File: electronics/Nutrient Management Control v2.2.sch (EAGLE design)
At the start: 16 parts, among them IC1 7407N, Q1 FQP30N06L

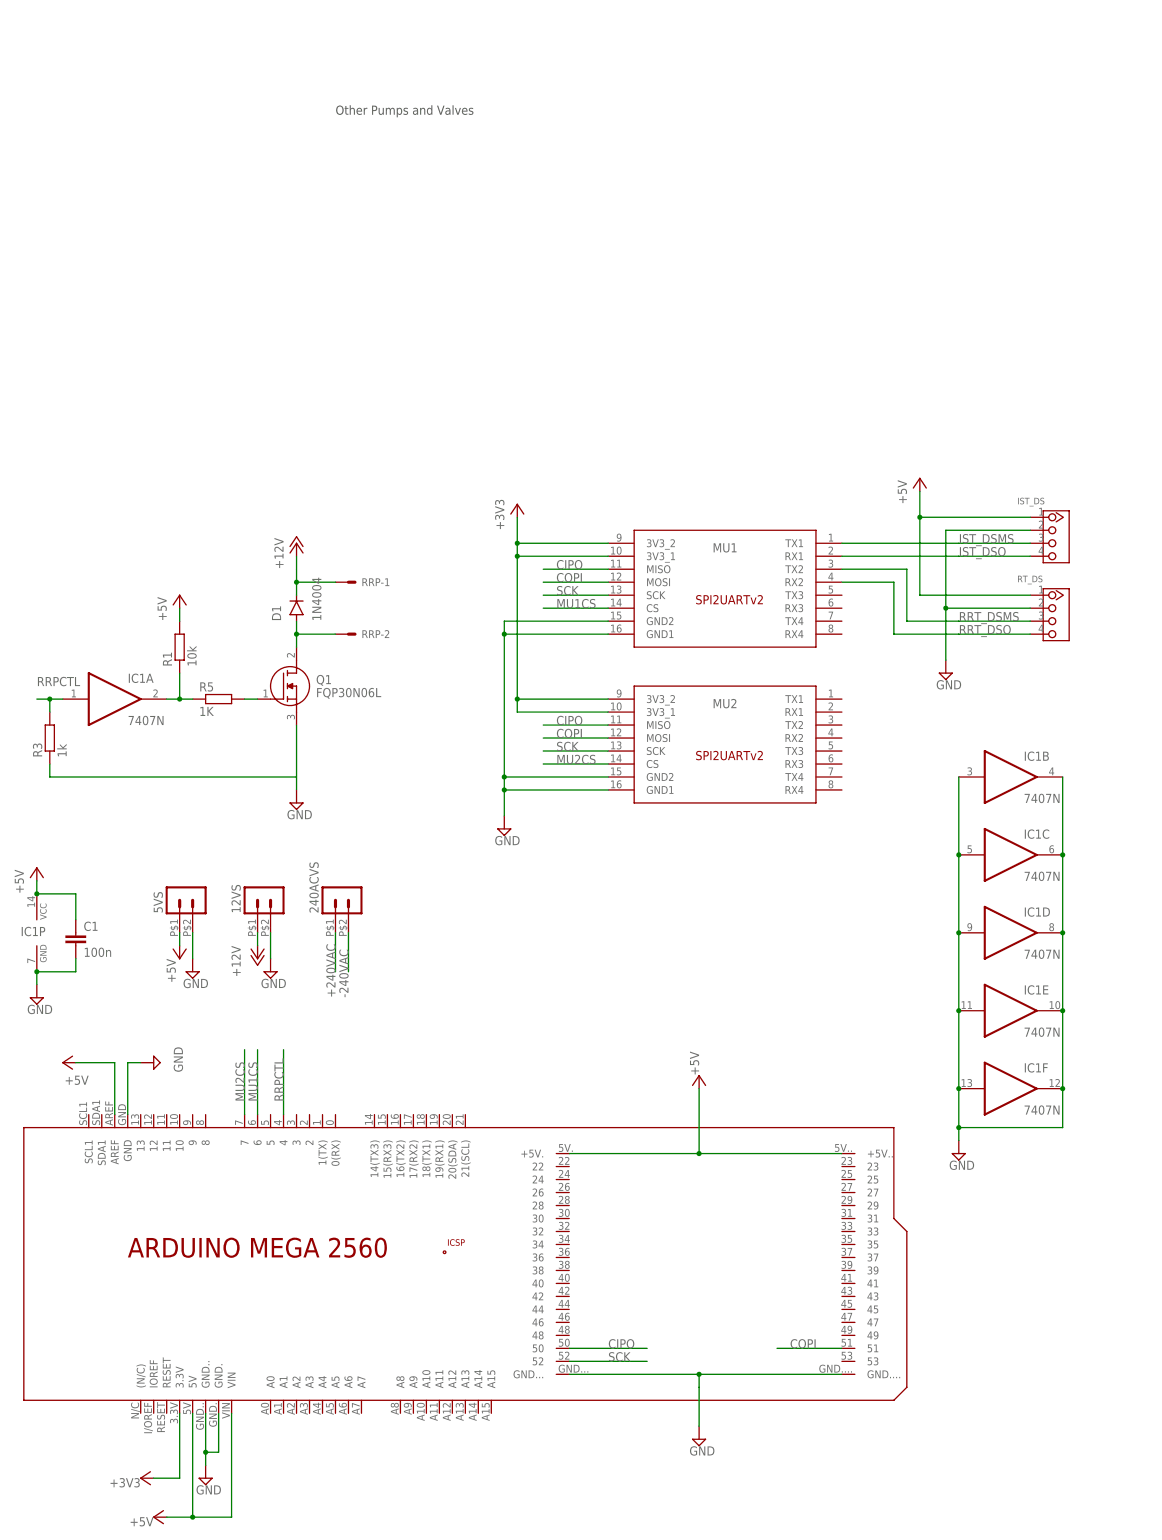
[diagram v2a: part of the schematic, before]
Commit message: Added UV Steriliser
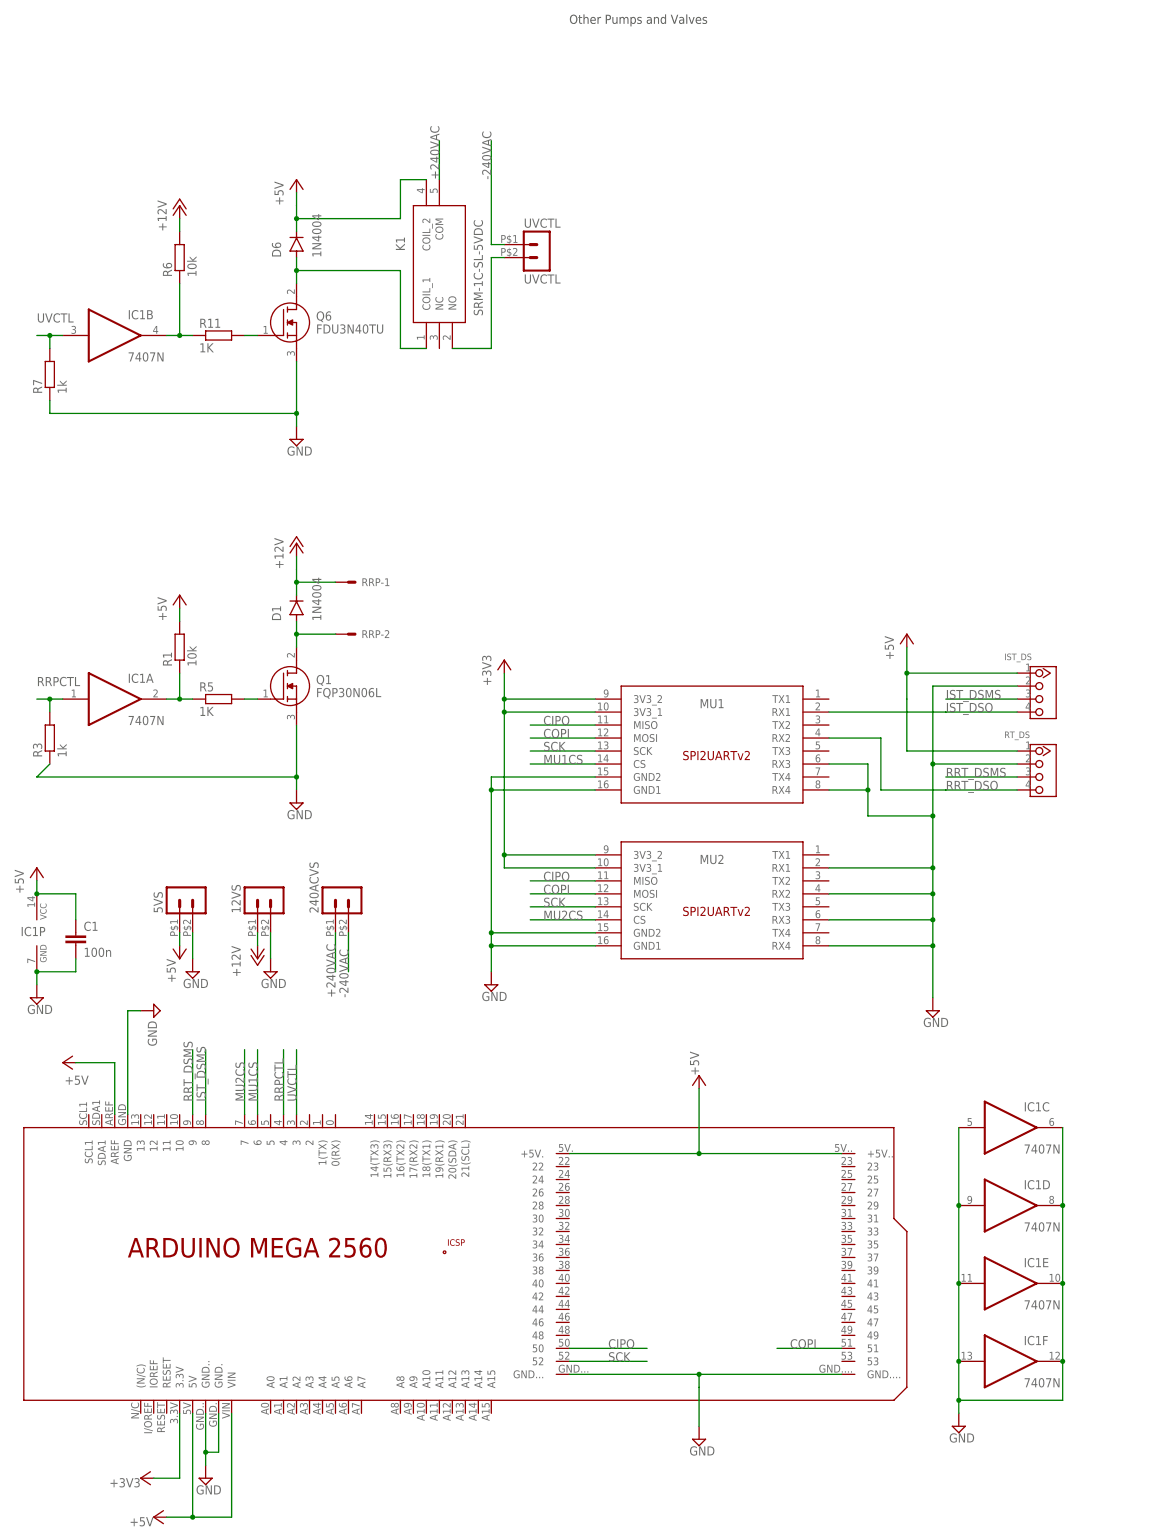
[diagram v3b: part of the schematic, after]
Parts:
- added D6: 1N4004, Aeroponics Control:1N4004
- added K1: SRM-1C-SL-5VDC, Aeroponics Control:SRM-1C-SL-5VDC
- added Q6: FDU3N40TU, Aeroponics Control:FDU3N40TU
- added R11: 1K, Aeroponics Control:R-EU_0204/7
- added R6: 10k, Aeroponics Control:R-EU_0204/7
- added R7: 1k, Aeroponics Control:R-EU_0204/7
- added UVCTL: UVCTL, Aeroponics Control:HEADER_POS2_43650-0215
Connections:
- new net N$13: Q6.G, R11.2
- new net N$17: IC1B.O, R11.1, R6.1
- new net N$21: D6.A, K1.COIL_1, Q6.D
- new net N$7: K1.NO, UVCTL.2
- new net UVCTL: IC1B.I, PCB2.3, R7.2
- net +12V: now also R6.2
- net +240VAC: now also K1.COM
- net +5V: now also D6.C, K1.COIL_2
- net -240VAC: now also UVCTL.1
- net GND: now also MU1.RX3, MU1.RX4, MU2.RX1, MU2.RX2, MU2.RX3, MU2.RX4, Q6.S, R7.1; no longer IC1B.I, IC1B.O
- net IST_DSMS: now also PCB2.8; no longer MU1.TX1
- net RRT_DSMS: now also PCB2.9; no longer MU1.TX2
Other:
- moved on the sheet: IC1B, IC1C, IC1D, IC1E, IC1F, IST_DS, MU1, MU2, RT_DS

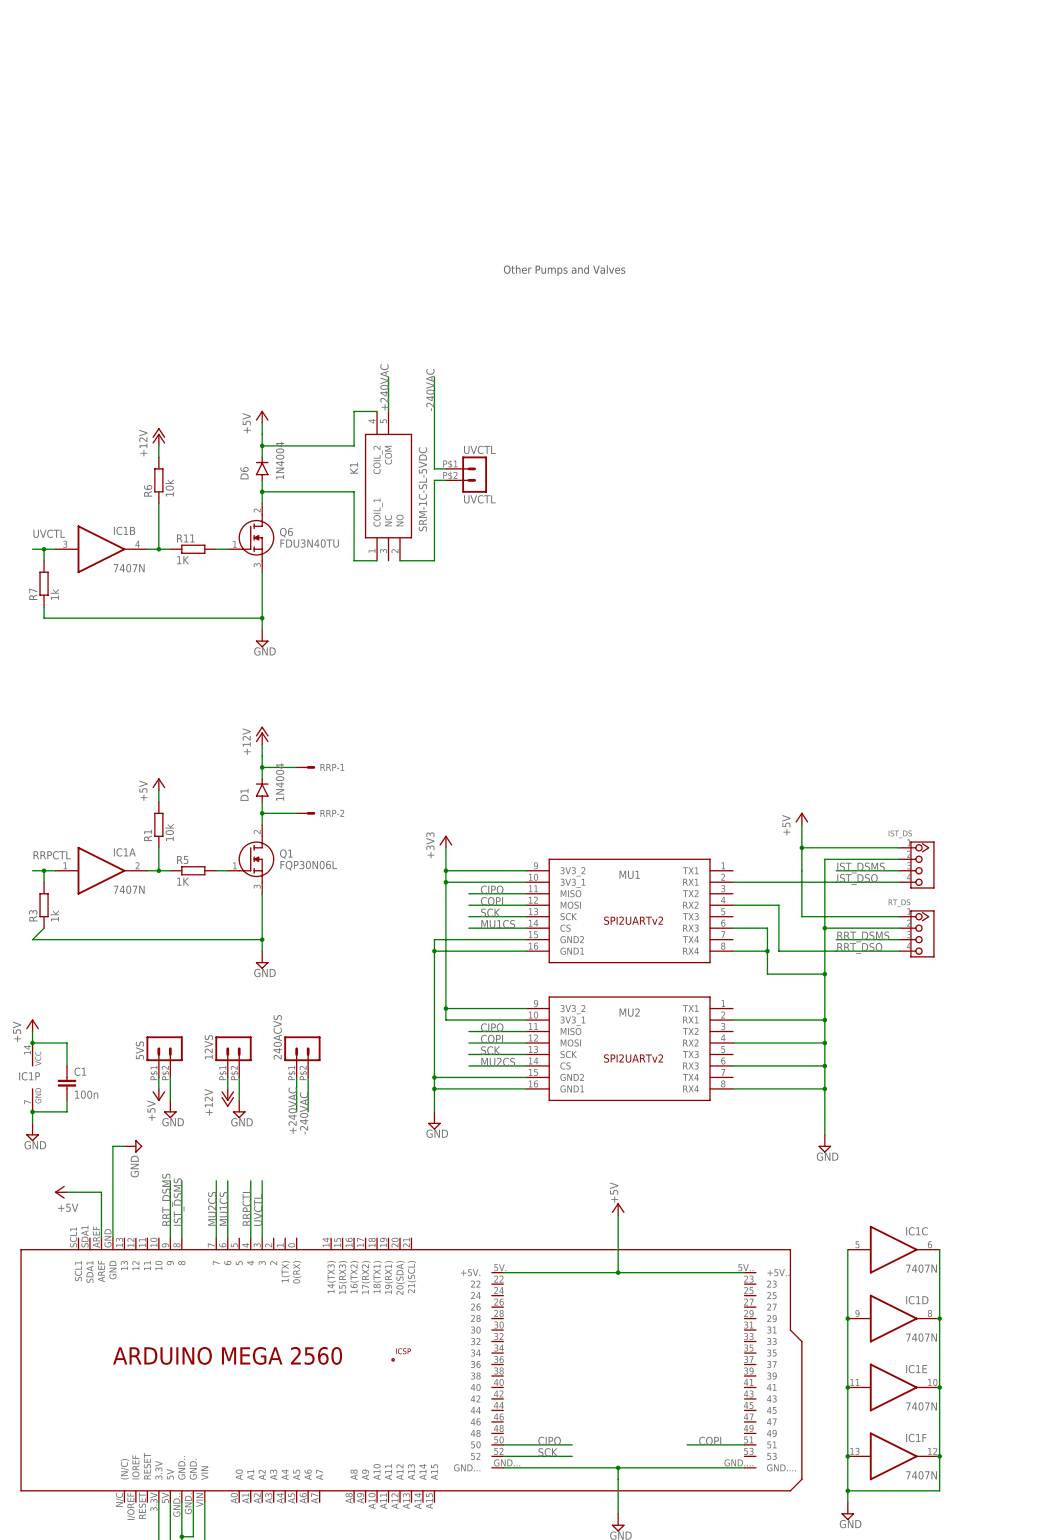
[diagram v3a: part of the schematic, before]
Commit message: Sorting out Nutrient Control Electronics
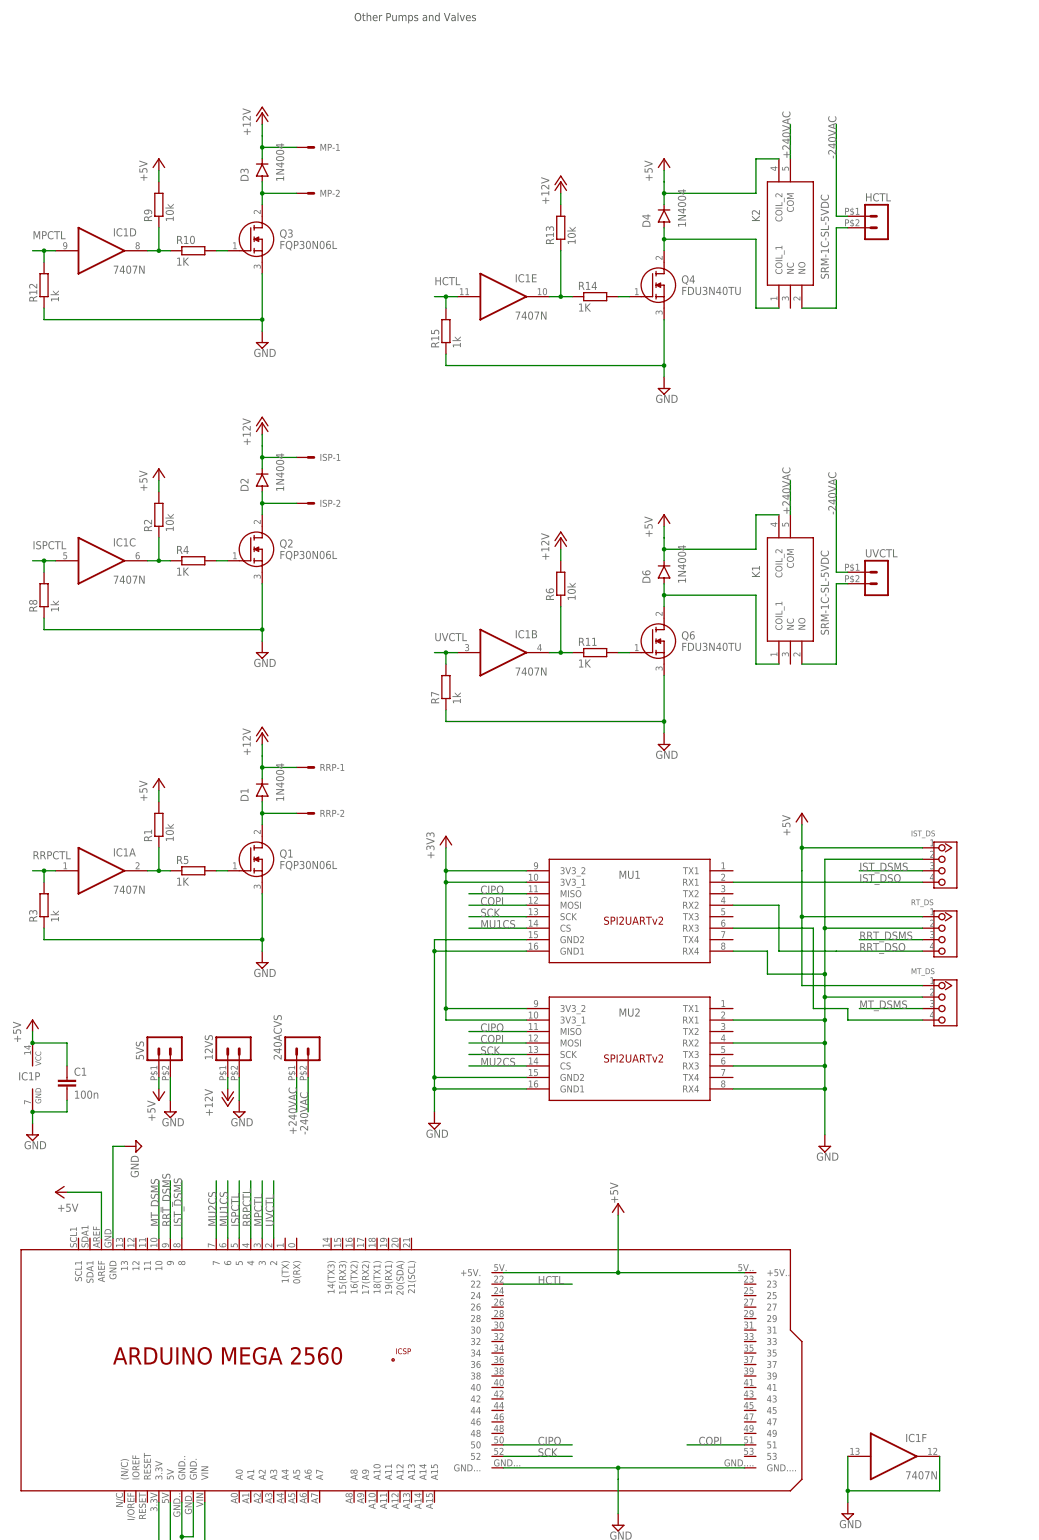
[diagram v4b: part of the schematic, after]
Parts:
- added D2, D3, D4: 1N4004, Aeroponics Control:1N4004
- added HCTL: (no value), Aeroponics Control:HEADER_POS2_43650-0215
- added ISP, MP: JST-XH-02-PIN-LONG-PAD, Aeroponics Control:JST-XH-02-PIN-LONG-PAD
- added K2: SRM-1C-SL-5VDC, Aeroponics Control:SRM-1C-SL-5VDC
- added MT_DS: 4P-2.0-90D, Aeroponics Control:GROVE-CONNECTOR-DIP-90D(4P-2.0)
- added Q2, Q3: FQP30N06L, Aeroponics Control:FQP30N06L
- added Q4: FDU3N40TU, Aeroponics Control:FDU3N40TU
- added R10, R14, R4: 1K, Aeroponics Control:R-EU_0204/7
- added R12, R15, R8: 1k, Aeroponics Control:R-EU_0204/7
- added R13, R2, R9: 10k, Aeroponics Control:R-EU_0204/7
- UVCTL: value UVCTL -> (none)
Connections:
- new net HCTL: IC1E.I, PCB2.22, R15.2
- new net ISPCTL: IC1C.I, PCB2.5, R8.2
- new net MPCTL: IC1D.I, PCB2.3, R12.2
- new net MT_DSMS: MT_DS.3, PCB2.10
- new net N$1: D2.A, ISP-2.S, Q2.D
- new net N$11: MT_DS.4, MU1.RX3
- new net N$12: D4.A, K2.COIL_1, Q4.D
- new net N$14: HCTL.2, K2.NO
- new net N$15: Q4.G, R14.2
- new net N$16: IC1E.O, R13.1, R14.1
- new net N$2: IC1C.O, R2.1, R4.1
- new net N$4: Q2.G, R4.2
- new net N$6: D3.A, MP-2.S, Q3.D
- new net N$8: IC1D.O, R10.1, R9.1
- new net N$9: Q3.G, R10.2
- net +12V: now also D2.C, D3.C, ISP-1.S, MP-1.S, R13.2
- net +240VAC: now also K2.COM
- net +5V: now also D4.C, K2.COIL_2, MT_DS.1, R2.2, R9.2
- net -240VAC: now also HCTL.1
- net GND: now also MT_DS.2, Q2.S, Q3.S, Q4.S, R12.1, R15.1, R8.1; no longer IC1C.I, IC1C.O, IC1D.I, IC1D.O, IC1E.I, IC1E.O, MU1.RX3
- net UVCTL: now also PCB2.2; no longer PCB2.3
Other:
- moved on the sheet: D6, IC1B, IC1C, IC1D, IC1E, IST_DS, K1, Q6, R11, R6, R7, RT_DS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
